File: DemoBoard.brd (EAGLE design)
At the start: 103.5 x 66.2 mm, 109 parts, among them IC1 LM20125MHE_NOPB, IC2 LM20125MHE_NOPB, J5 DM3AT-SF-PEJM5, J6 SAMTEC-MMS-105-02-X-SVJ, Q1 IRLML0030TRPBF, Q2 MMBT3904,215, Q3 MMBT3904,215, Q4 BC846B,235, Q5 BC846B,235, Q6 BC846B,235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

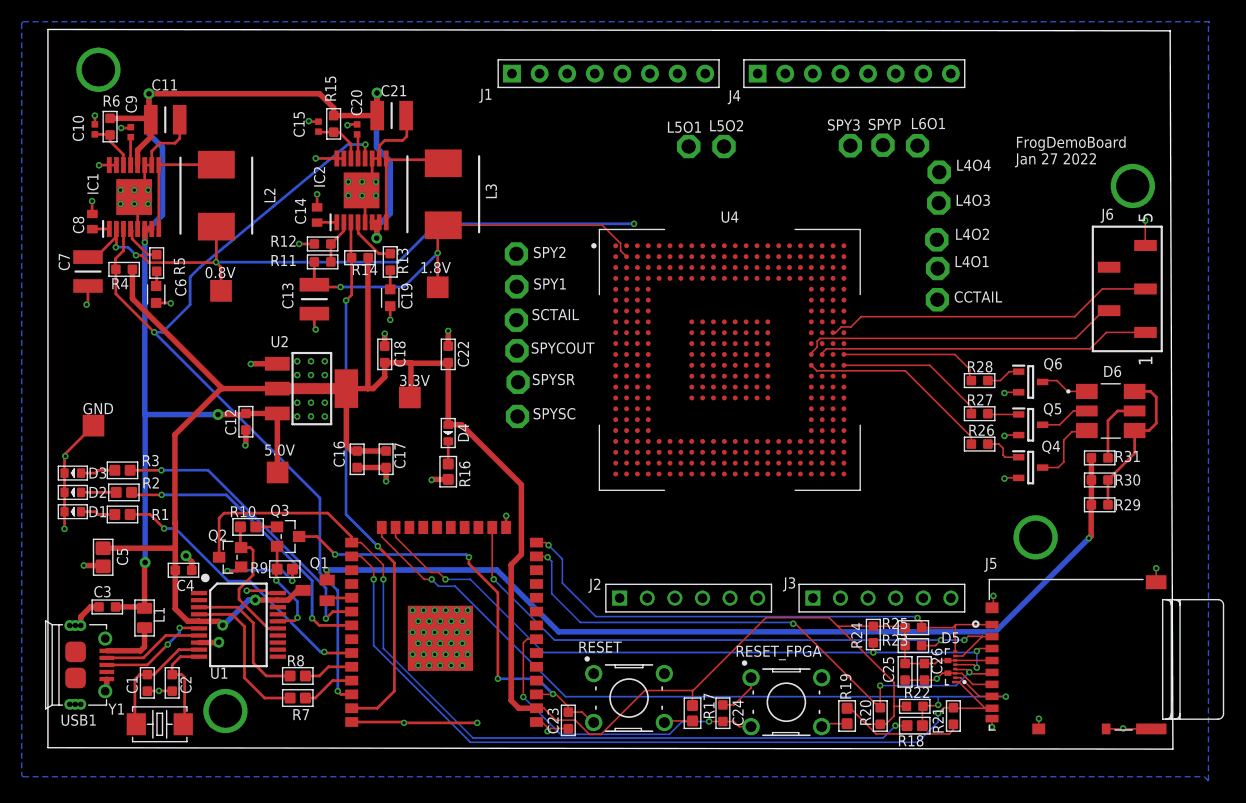
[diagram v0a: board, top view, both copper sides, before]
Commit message: Finalize routing, DRC Clean
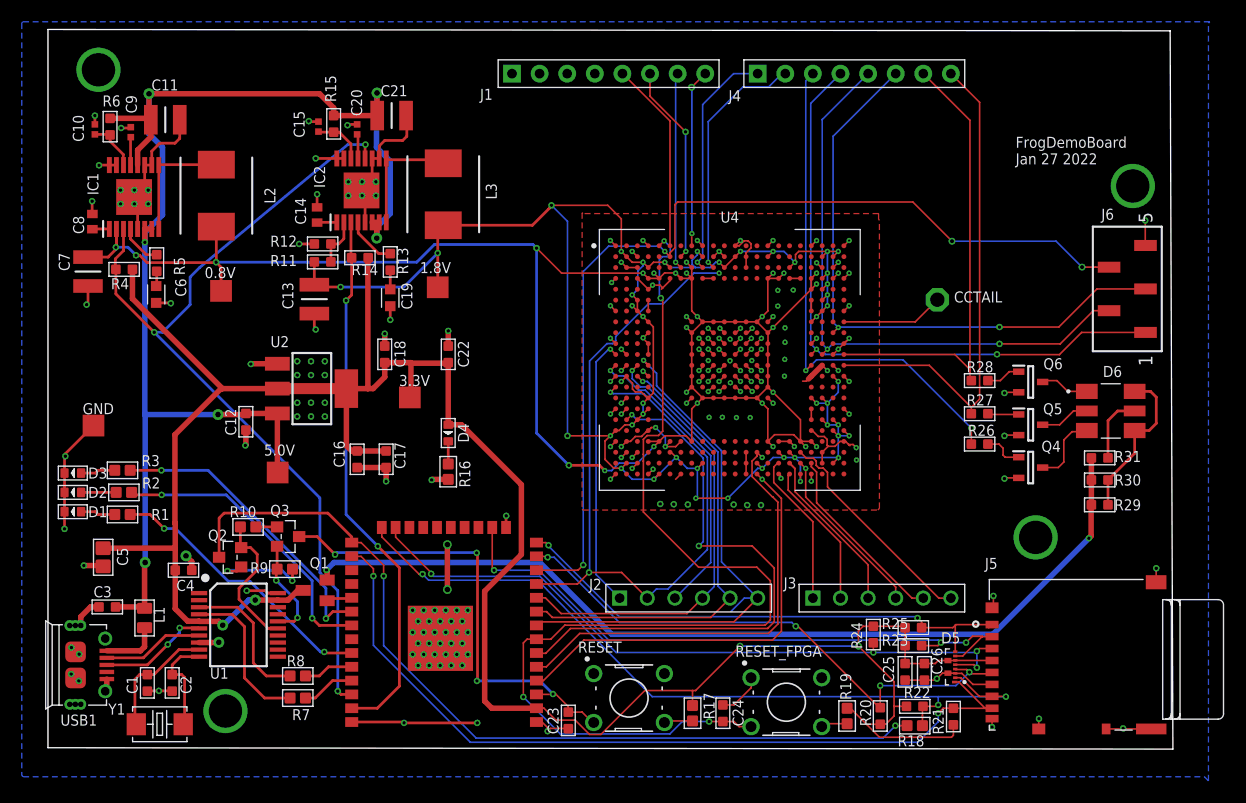
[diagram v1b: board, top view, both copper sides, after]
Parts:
- removed L4O1, L4O2, L4O3, L4O4, L5O1, L5O2, L6O1, SCTAIL, SPY1, SPY2, SPY3, SPYCOUT, SPYP, SPYSC, SPYSR: TPPAD1-13, testpad:P1-13
- moved R21 0.05 mm to (83.3, 2.87)
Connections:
- removed net SC_HEAD: U3.27, U4.H20
- removed net TEST_EN: U3.11, U4.D11
- new net N$72: USB1.4
- new net N$73: U3.27
- new net N$74: U4.D11
- new net N$75: U3.28
- net GPIO18: now also J4.3
- net GPIO19: no longer J4.3
- net GPIO21: now also J6.1; no longer J6.2
- net GPIO22: now also J6.2; no longer J6.1
- net GPIO6: now also U3.9; no longer U3.8
- net GPIO7: now also U3.11; no longer U3.28
- net GPIO8: now also U3.10; no longer U3.9
- net GPIO9: now also U3.8; no longer U3.10
- net N$10: now also U4.C12; no longer L5O2.TP, U4.B5
- net N$11: now also U4.P2; no longer L6O1.TP, U4.C12
- net N$15: now also U4.A10; no longer SPY2.TP, U4.P2
- net N$16: now also U4.R3; no longer SPY3.TP, U4.A10
- net N$18: now also U4.U1; no longer SPY1.TP, U4.R3
- net N$19: now also U4.V3; no longer SPYCOUT.TP, U4.U1
- net N$21: now also U4.H20; no longer SPYSC.TP, U4.V3
- net N$23: no longer SPYSR.TP
- net N$24: no longer SPYP.TP
- net N$4: no longer L4O4.TP
- net N$5: no longer L4O2.TP
- net N$6: no longer L4O3.TP
- net N$61: no longer SCTAIL.TP
- net N$8: no longer L4O1.TP
- net N$9: no longer L5O1.TP
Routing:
- net 1.8V: track 39.2 -> 184.7 mm, vias 2 -> 45
- net 0.8V: track 61.5 -> 175.6 mm, vias 4 -> 27
- net GND: track 124.3 -> 225.5 mm, vias 97 -> 209
- net CLK: track 0.00 -> 89.1 mm, vias 0 -> 4
- net GPIO7: track 0.00 -> 74.5 mm, vias 0 -> 3
- net RESET_FPGA: track 29.4 -> 97.5 mm, vias 2 -> 4
- net CCFF_HEAD: track 0.00 -> 53.0 mm, vias 0 -> 2
- net GPIO9: track 0.00 -> 51.2 mm, vias 0 -> 1
- net GPIO6: track 0.00 -> 43.0 mm, vias 0 -> 1
- net GPIO8: track 0.00 -> 42.1 mm, vias 0 -> 1
- net P_RESET: track 0.00 -> 41.6 mm, vias 0 -> 1
- net PROG_CLK: track 0.00 -> 39.8 mm, vias 0 -> 1
- net GPIO19: track 13.9 -> 46.2 mm
- net GPIO18: track 18.1 -> 48.0 mm, vias 0 -> 2
- net GPIO21: track 29.5 -> 58.8 mm, vias 0 -> 2
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- added copper zone on layer 1, net GND
